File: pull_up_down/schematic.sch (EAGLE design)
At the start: 2 parts

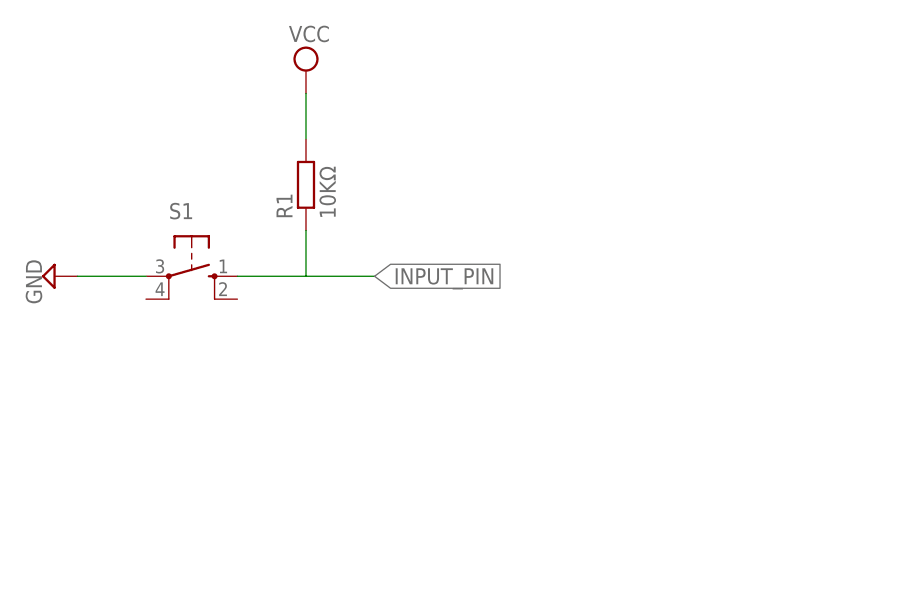
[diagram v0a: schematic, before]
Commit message: add pull-up/pull-down resistor circuit and voltage divider circuit
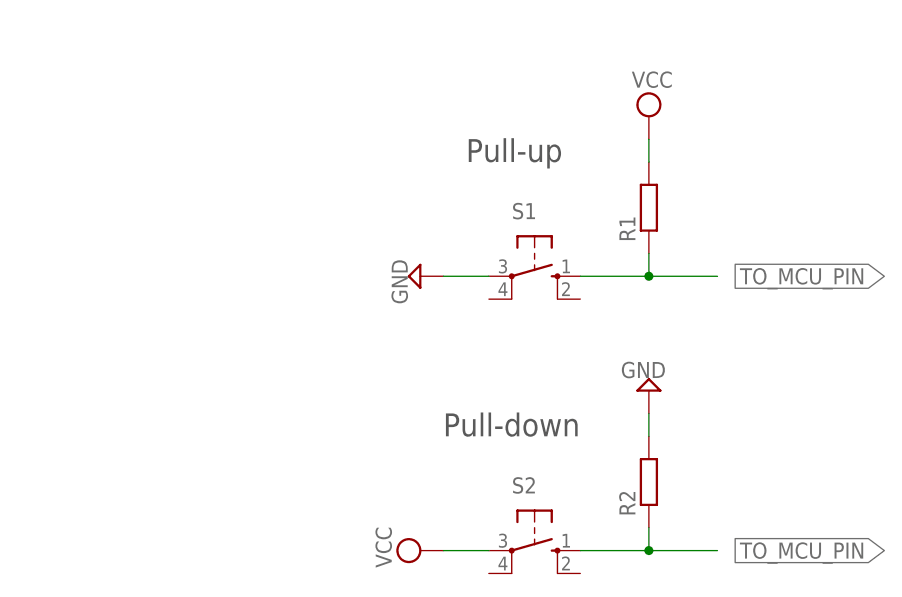
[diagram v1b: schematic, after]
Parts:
- added R2: (no value), eagle-ltspice:R0204/7
- added S2: (no value), switch-omron:10-XX
- R1: value 10KΩ -> (none); device eagle-ltspice:R0207/10 -> eagle-ltspice:R0204/7
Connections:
- removed net INPUT_PIN: R1.1, S1.S
- new net TO_MCU_PIN: R1.1, R2.1, S1.S, S2.S
- net GND: now also R2.2; no longer S1.P
- net VCC: now also S2.P
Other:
- note added: "Pull-down"
- note added: "Pull-up"
- moved on the sheet: R1, S1
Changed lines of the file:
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@@
 <layer number="51" name="tDocu" color="7" fill="1" visible="no" active="no"/>
 <layer number="52" name="bDocu" color="7" fill="1" visible="no" active="no"/>
-<layer number="90" name="Modules" color="5" fill="1" visible="yes" active="yes"/>
+<layer number="90" name="Modules" color="5" fill="1" visible="no" active="yes"/>
 <layer number="91" name="Nets" color="2" fill="1" visible="yes" active="yes"/>
 <layer number="92" name="Busses" color="1" fill="1" visible="yes" active="yes"/>
@@
 <layer number="97" name="Info" color="7" fill="1" visible="yes" active="yes"/>
 <layer number="98" name="Guide" color="6" fill="1" visible="yes" active="yes"/>
-<layer number="99" name="SpiceOrder" color="5" fill="1" visible="yes" active="yes"/>
+<layer number="99" name="SpiceOrder" color="5" fill="1" visible="no" active="yes"/>
 </layers>
 <schematic xreflabel="%F%N/%S.%C%R" xrefpart="/%S.%C%R">
@@
 <parts>
 <part name="SUPPLY1" library="supply2" deviceset="GND" device=""/>
-<part name="SUPPLY3" library="supply2" deviceset="VCC" device=""/>
+<part name="SUPPLY2" library="supply2" deviceset="VCC" device=""/>
+<part name="R1" library="eagle-ltspice" deviceset="R" device="0204/7"/>
 <part name="S1" library="switch-omron" deviceset="10-XX" device=""/>
-<part name="R1" library="eagle-ltspice" deviceset="R" device="0207/10" value="10KΩ"/>
+<part name="SUPPLY3" library="supply2" deviceset="GND" device=""/>
+<part name="SUPPLY4" library="supply2" deviceset="VCC" device=""/>
+<part name="R2" library="eagle-ltspice" deviceset="R" device="0204/7"/>
+<part name="S2" library="switch-omron" deviceset="10-XX" device=""/>
 </parts>
 <sheets>
 <sheet>
 <plain>
+<text x="43.18" y="55.88" size="2.54" layer="97">Pull-up</text>
+<text x="40.64" y="25.4" size="2.54" layer="97">Pull-down</text>
 </plain>
 <instances>
-<instance part="SUPPLY1" gate="GND" x="-2.54" y="43.18" rot="R270"/>
-<instance part="SUPPLY3" gate="G$1" x="25.4" y="66.04"/>
-<instance part="S1" gate="1" x="12.7" y="43.18" rot="R270"/>
-<instance part="R1" gate="G$1" x="25.4" y="53.34" rot="R90"/>
+<instance part="SUPPLY1" gate="GND" x="38.1" y="43.18" rot="R270"/>
+<instance part="SUPPLY2" gate="G$1" x="63.5" y="60.96"/>
+<instance part="R1" gate="G$1" x="63.5" y="50.8" rot="R90"/>
+<instance part="S1" gate="1" x="50.8" y="43.18" rot="R270"/>
+<instance part="SUPPLY3" gate="GND" x="63.5" y="30.48" rot="R180"/>
+<instance part="SUPPLY4" gate="G$1" x="38.1" y="12.7" rot="R90"/>
+<instance part="R2" gate="G$1" x="63.5" y="20.32" rot="R90"/>
+<instance part="S2" gate="1" x="50.8" y="12.7" rot="R270"/>
 </instances>
 <busses>
@@
 <segment>
 <pinref part="SUPPLY1" gate="GND" pin="GND"/>
-<pinref part="S1" gate="1" pin="P"/>
-<wire x1="0" y1="43.18" x2="7.62" y2="43.18" width="0.1524" layer="91"/>
+<wire x1="45.72" y1="43.18" x2="40.64" y2="43.18" width="0.1524" layer="91"/>
 </segment>
-</net>
-<net name="INPUT_PIN" class="0">
 <segment>
-<pinref part="S1" gate="1" pin="S"/>
-<wire x1="17.78" y1="43.18" x2="25.4" y2="43.18" width="0.1524" layer="91"/>
-<pinref part="R1" gate="G$1" pin="1"/>
-<wire x1="25.4" y1="43.18" x2="33.02" y2="43.18" width="0.1524" layer="91"/>
-<wire x1="25.4" y1="48.26" x2="25.4" y2="43.18" width="0.1524" layer="91"/>
-<label x="33.02" y="43.18" size="1.778" layer="95" rot="MR180" xref="yes"/>
+<pinref part="SUPPLY3" gate="GND" pin="GND"/>
+<pinref part="R2" gate="G$1" pin="2"/>
+<wire x1="63.5" y1="27.94" x2="63.5" y2="25.4" width="0.1524" layer="91"/>
 </segment>
 </net>
 <net name="VCC" class="0">
 <segment>
-<pinref part="SUPPLY3" gate="G$1" pin="VCC"/>
+<pinref part="SUPPLY2" gate="G$1" pin="VCC"/>
 <pinref part="R1" gate="G$1" pin="2"/>
-<wire x1="25.4" y1="63.5" x2="25.4" y2="58.42" width="0.1524" layer="91"/>
+<wire x1="63.5" y1="55.88" x2="63.5" y2="58.42" width="0.1524" layer="91"/>
+</segment>
+<segment>
+<pinref part="SUPPLY4" gate="G$1" pin="VCC"/>
+<pinref part="S2" gate="1" pin="P"/>
+<wire x1="40.64" y1="12.7" x2="45.72" y2="12.7" width="0.1524" layer="91"/>
 </segment>
 </net>
+<net name="TO_MCU_PIN" class="0">
+<segment>
+<pinref part="S1" gate="1" pin="S"/>
+<wire x1="55.88" y1="43.18" x2="63.5" y2="43.18" width="0.1524" layer="91"/>
+<pinref part="R1" gate="G$1" pin="1"/>
+<wire x1="63.5" y1="43.18" x2="71.12" y2="43.18" width="0.1524" layer="91"/>
+<wire x1="63.5" y1="45.72" x2="63.5" y2="43.18" width="0.1524" layer="91"/>
+<junction x="63.5" y="43.18"/>
+<label x="89.662" y="43.18" size="1.778" layer="95" rot="MR0" xref="yes"/>
+</segment>
+<segment>
+<pinref part="S2" gate="1" pin="S"/>
+<wire x1="55.88" y1="12.7" x2="63.5" y2="12.7" width="0.1524" layer="91"/>
+<pinref part="R2" gate="G$1" pin="1"/>
+<wire x1="63.5" y1="12.7" x2="71.12" y2="12.7" width="0.1524" layer="91"/>
+<wire x1="63.5" y1="15.24" x2="63.5" y2="12.7" width="0.1524" layer="91"/>
+<junction x="63.5" y="12.7"/>
+<label x="89.662" y="12.7" size="1.778" layer="95" rot="MR0" xref="yes"/>
+</segment>
+</net>
